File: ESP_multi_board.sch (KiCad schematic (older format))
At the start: 20 parts, among them P101 CONN_01X02, P102 CONN_01X06, P103 CONN_01X02, P104 CONN_01X06, P105 CONN_01X12, P106 CONN_01X03, P108 CONN_I2C_MPU6050, P109 CONN_01X03, P110 CONN_01X03, P111 CONN_DIGITAL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

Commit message: incluido DAC 4canales MCP4728, modificados conexion de motores para hacer pwm en los enables
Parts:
- removed P109, P110: CONN_01X03, Pin_Headers:Pin_Header_Straight_1x03, symbol CONN_01X03
- removed P111: CONN_DIGITAL, Pin_Headers:Pin_Header_Straight_1x10, symbol CONN_01X10
- removed P112: CONN_I2C, Pin_Headers:Pin_Header_Straight_1x04, symbol CONN_01X04
- added C?: CP, symbol CP
- added C?: 0.1u, symbol C
- added C?: 10u, symbol CP
- added P?: CONN_PWM_OUT, symbol CONN_01X04
- added P?: CONN_PWM_VCC, symbol CONN_01X04
- added P?: CONN_PWM_GND, symbol CONN_01X04
- added P?: CONN_PINES_DIG, symbol CONN_01X06
- added R?: 100k, symbol R
- added U?: MCP4728-E/UN, MSOP-10, symbol MCP4728-E/UN
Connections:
- net labels added: EN1, EN2
- wire segments 94 -> 110
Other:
- moved on the sheet: JP101, P106, P108, R101, R102, R103, R104, U102

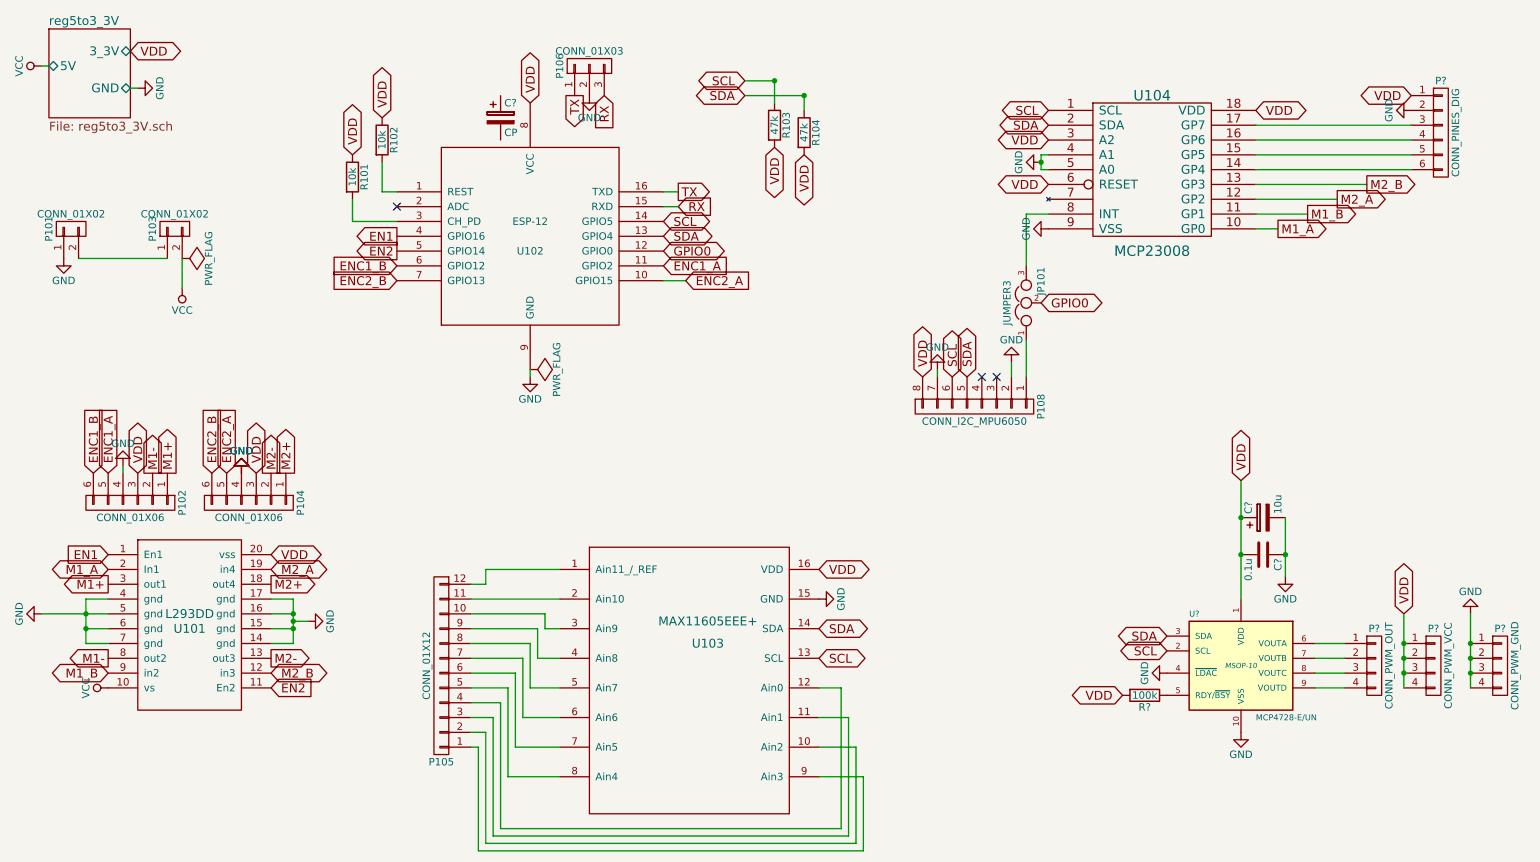
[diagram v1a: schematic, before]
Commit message: modificada huella del jumper, incluidos condensadores en la linea de 3.3v
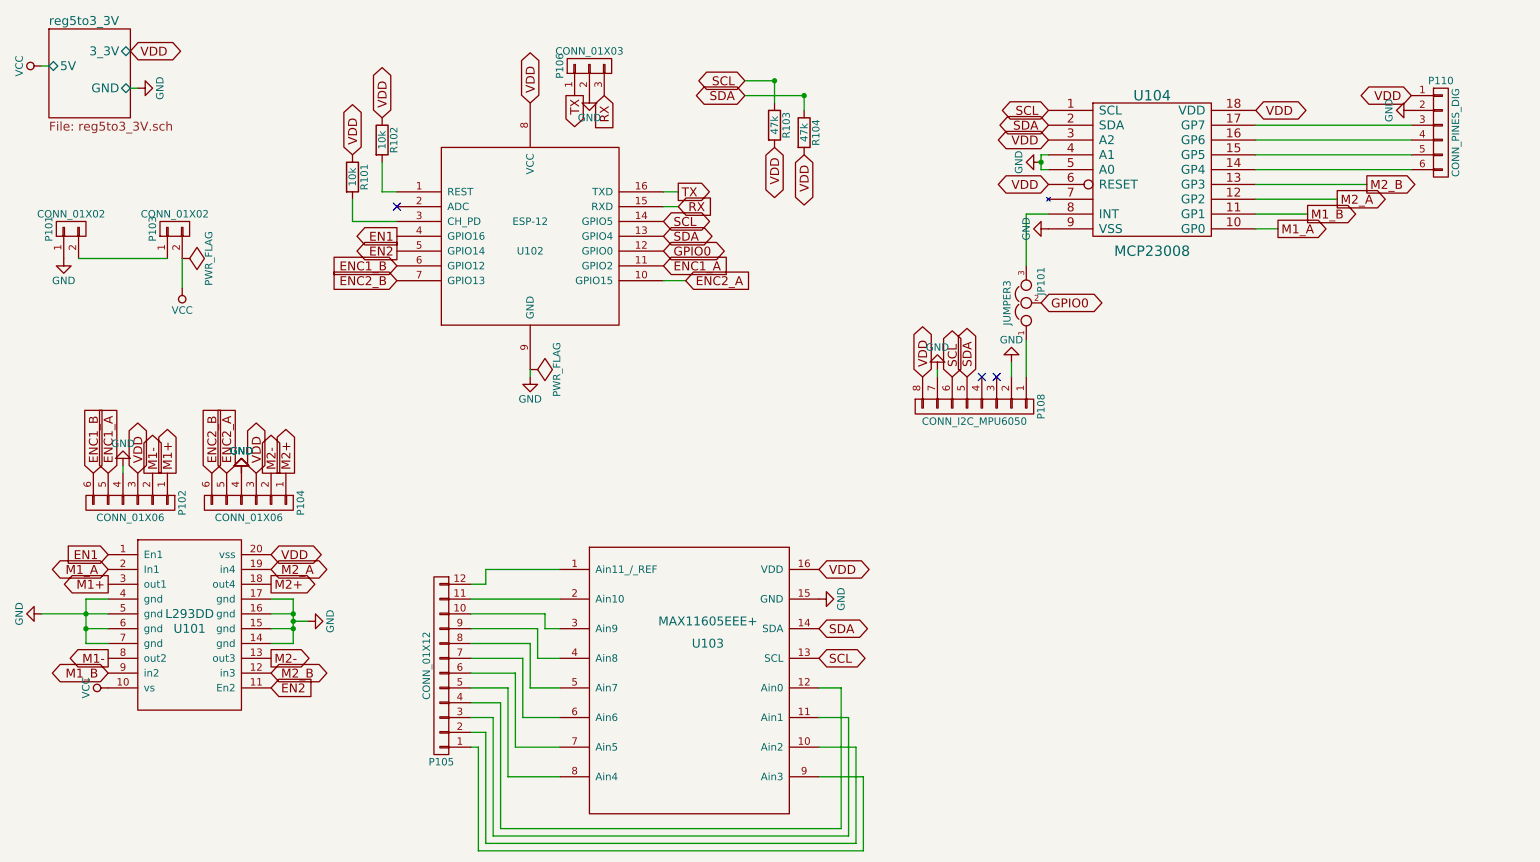
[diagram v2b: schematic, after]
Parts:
- removed C?: CP, symbol CP
- removed C?: 0.1u, symbol C
- removed C?: 10u, symbol CP
- removed P?: CONN_PWM_OUT, symbol CONN_01X04
- removed P?: CONN_PWM_VCC, symbol CONN_01X04
- removed P?: CONN_PWM_GND, symbol CONN_01X04
- removed R?: 100k, symbol R
- removed U?: MCP4728-E/UN, MSOP-10, symbol MCP4728-E/UN
- U103: footprint Housings_SSOP:QSOP-16_3.9x4.9mm_Pitch0.635mm -> Housings_SSOP:SSOP-16_5.3x6.2mm_Pitch0.65mm
- gave numbers to parts that had none: 1

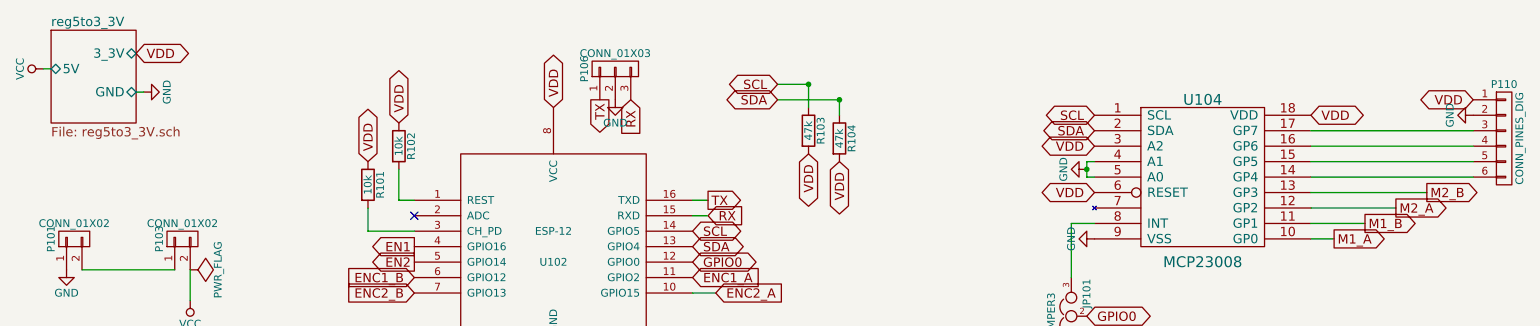
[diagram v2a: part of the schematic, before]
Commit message: autorouting generado con freerouting
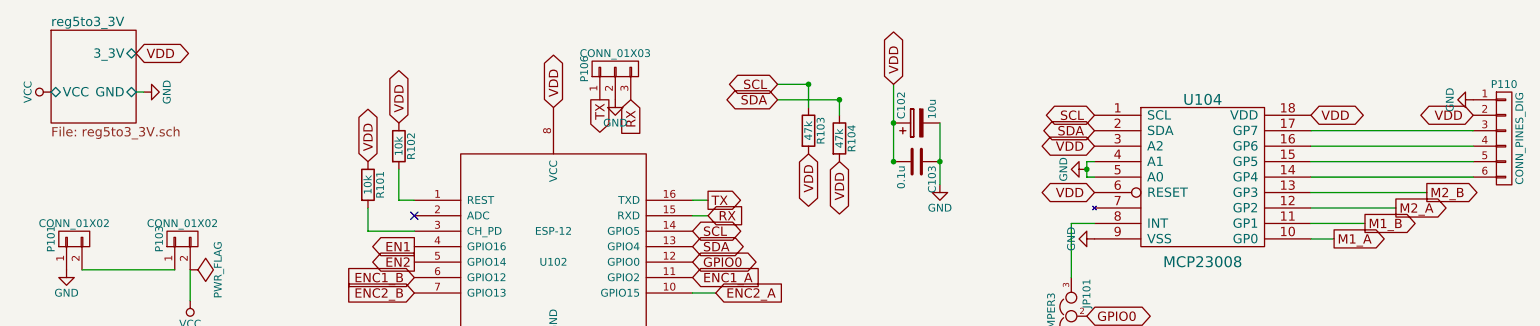
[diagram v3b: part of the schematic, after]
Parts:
- added C102: 10u, Capacitors_Tantalum_SMD:TantalC_SizeC_EIA-6032_HandSoldering, symbol CP
- added C103: 0.1u, Capacitors_SMD:C_0805_HandSoldering, symbol C
- JP101: footprint Oddities:NetTie-II_SMD -> keyboard_parts:SOLDER_JUMPER_3
- P110: footprint (none) -> Pin_Headers:Pin_Header_Straight_1x06
- R101, R102, R103, R104: footprint Resistors_SMD:R_1812_HandSoldering -> Resistors_SMD:R_0805_HandSoldering
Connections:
- net GND: now also P110.1 (P1), C102.2, C103.1; no longer P110.2 (P2)
- net VDD: now also P110.2 (P2), C102.1, C103.2; no longer P110.1 (P1)
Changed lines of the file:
@@
 L VCC #PWR06
 U 1 1 57125BE7
-P 950 1050
-F 0 "#PWR06" H 950 900 50  0001 C CNN
-F 1 "VCC" H 950 1200 50  0000 C CNN
-F 2 "" H 950 1050 50  0000 C CNN
-F 3 "" H 950 1050 50  0000 C CNN
-	1    950  1050
+P 1000 1200
+F 0 "#PWR06" H 1000 1050 50  0001 C CNN
+F 1 "VCC" H 1000 1350 50  0000 C CNN
+F 2 "" H 1000 1200 50  0000 C CNN
+F 3 "" H 1000 1200 50  0000 C CNN
+	1    1000 1200
 	0    -1   -1   0
 $EndComp
@@
 F1 "reg5to3_3V.sch" 60
 F2 "GND" B R 1550 1200 60
-F3 "5V" B L 1000 1050 60
-F4 "3_3V" B R 1550 950 60
+F3 "3_3V" B R 1550 950 60
+F4 "VCC" B L 1000 1200 60
 $EndSheet
 $Comp
@@
 F 0 "R102" V 3330 1550 50  0000 C CNN
 F 1 "10k" V 3250 1550 50  0000 C CNN
-F 2 "Resistors_SMD:R_1812_HandSoldering" V 3180 1550 50  0001 C CNN
+F 2 "Resistors_SMD:R_0805_HandSoldering" V 3180 1550 50  0001 C CNN
 F 3 "" H 3250 1550 50  0000 C CNN
 	1    3250 1550
@@
 F 0 "R101" V 3130 1800 50  0000 C CNN
 F 1 "10k" V 3050 1800 50  0000 C CNN
-F 2 "Resistors_SMD:R_1812_HandSoldering" V 2980 1800 50  0001 C CNN
+F 2 "Resistors_SMD:R_0805_HandSoldering" V 2980 1800 50  0001 C CNN
 F 3 "" H 3050 1800 50  0000 C CNN
 	1    3050 1800
@@
 F 0 "R104" V 6180 1500 50  0000 C CNN
 F 1 "47k" V 6100 1500 50  0000 C CNN
-F 2 "Resistors_SMD:R_1812_HandSoldering" V 6030 1500 50  0001 C CNN
+F 2 "Resistors_SMD:R_0805_HandSoldering" V 6030 1500 50  0001 C CNN
 F 3 "" H 6100 1500 50  0000 C CNN
 	1    6100 1500
@@
 F 0 "R103" V 5980 1450 50  0000 C CNN
 F 1 "47k" V 5900 1450 50  0000 C CNN
-F 2 "Resistors_SMD:R_1812_HandSoldering" V 5830 1450 50  0001 C CNN
+F 2 "Resistors_SMD:R_0805_HandSoldering" V 5830 1450 50  0001 C CNN
 F 3 "" H 5900 1450 50  0000 C CNN
 	1    5900 1450
@@
 Text GLabel 5150 2400 2    60   Input ~ 0
 ENC1_A
-Text GLabel 10200 1250 0    60   BiDi ~ 0
+Text GLabel 10200 1350 0    60   BiDi ~ 0
 VDD
 Text GLabel 1800 3800 1    60   Output ~ 0
@@
 L GND #PWR010
 U 1 1 57143D77
-P 10200 1350
-F 0 "#PWR010" H 10200 1100 50  0001 C CNN
-F 1 "GND" H 10200 1200 50  0000 C CNN
-F 2 "" H 10200 1350 50  0000 C CNN
-F 3 "" H 10200 1350 50  0000 C CNN
-	1    10200 1350
+P 10200 1250
+F 0 "#PWR010" H 10200 1000 50  0001 C CNN
+F 1 "GND" H 10200 1100 50  0000 C CNN
+F 2 "" H 10200 1250 50  0000 C CNN
+F 3 "" H 10200 1250 50  0000 C CNN
+	1    10200 1250
 	0    1    1    0
 $EndComp
@@
 	7600 2900 7600 3150
 Wire Wire Line
-	1000 1050 950  1050
-Wire Wire Line
 	1550 1200 1600 1200
 Wire Wire Line
@@
 F 0 "JP101" H 7650 2550 50  0000 L CNN
 F 1 "JUMPER3" H 7600 2750 50  0000 C BNN
-F 2 "Oddities:NetTie-II_SMD" H 7600 2650 50  0001 C CNN
+F 2 "keyboard_parts:SOLDER_JUMPER_3" H 7600 2650 50  0001 C CNN
 F 3 "" H 7600 2650 50  0000 C CNN
 	1    7600 2650
@@
 F 0 "P110" H 10400 1850 50  0000 C CNN
 F 1 "CONN_PINES_DIG" V 10500 1500 50  0000 C CNN
-F 2 "" H 10400 1500 50  0001 C CNN
+F 2 "Pin_Headers:Pin_Header_Straight_1x06" H 10400 1500 50  0001 C CNN
 F 3 "" H 10400 1500 50  0000 C CNN
 	1    10400 1500
 	1    0    0    -1
 $EndComp
+$Comp
+L GND #PWR021
+U 1 1 57154834
+P 6750 1800
+F 0 "#PWR021" H 6750 1550 50  0001 C CNN
+F 1 "GND" H 6750 1650 50  0000 C CNN
+F 2 "" H 6750 1800 50  0000 C CNN
+F 3 "" H 6750 1800 50  0000 C CNN
+	1    6750 1800
+	1    0    0    -1
+$EndComp
+Connection ~ 6750 1650
+Wire Wire Line
+	6750 1400 6750 1800
+Text GLabel 6450 1150 1    60   BiDi ~ 0
+VDD
+Connection ~ 6450 1400
+Connection ~ 6450 1650
+$Comp
+L CP C102
+U 1 1 5715447A
+P 6600 1400
+F 0 "C102" H 6625 1500 50  0000 L CNN
+F 1 "10u" H 6625 1300 50  0000 L CNN
+F 2 "Capacitors_Tantalum_SMD:TantalC_SizeC_EIA-6032_HandSoldering" H 6638 1250 50  0001 C CNN
+F 3 "" H 6600 1400 50  0000 C CNN
+	1    6600 1400
+	0    -1   -1   0
+$EndComp
+$Comp
+L C C103
+U 1 1 57154411
+P 6600 1650
+F 0 "C103" H 6625 1750 50  0000 L CNN
+F 1 "0.1u" H 6625 1550 50  0000 L CNN
+F 2 "Capacitors_SMD:C_0805_HandSoldering" H 6638 1500 50  0001 C CNN
+F 3 "" H 6600 1650 50  0000 C CNN
+	1    6600 1650
+	0    1    1    0
+$EndComp
+Wire Wire Line
+	6450 1150 6450 1650
 $EndSCHEMATC

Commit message: cambio de posiciones en la placa
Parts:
- C103: footprint Capacitors_SMD:C_0805_HandSoldering -> Capacitors_SMD:C_1206
- R101, R102, R103, R104: footprint Resistors_SMD:R_0805_HandSoldering -> Resistors_SMD:R_1206
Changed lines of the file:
@@
 F 0 "R102" V 3330 1550 50  0000 C CNN
 F 1 "10k" V 3250 1550 50  0000 C CNN
-F 2 "Resistors_SMD:R_0805_HandSoldering" V 3180 1550 50  0001 C CNN
+F 2 "Resistors_SMD:R_1206" V 3180 1550 50  0001 C CNN
 F 3 "" H 3250 1550 50  0000 C CNN
 	1    3250 1550
@@
 F 0 "R101" V 3130 1800 50  0000 C CNN
 F 1 "10k" V 3050 1800 50  0000 C CNN
-F 2 "Resistors_SMD:R_0805_HandSoldering" V 2980 1800 50  0001 C CNN
+F 2 "Resistors_SMD:R_1206" V 2980 1800 50  0001 C CNN
 F 3 "" H 3050 1800 50  0000 C CNN
 	1    3050 1800
@@
 F 0 "R104" V 6180 1500 50  0000 C CNN
 F 1 "47k" V 6100 1500 50  0000 C CNN
-F 2 "Resistors_SMD:R_0805_HandSoldering" V 6030 1500 50  0001 C CNN
+F 2 "Resistors_SMD:R_1206" V 6030 1500 50  0001 C CNN
 F 3 "" H 6100 1500 50  0000 C CNN
 	1    6100 1500
@@
 F 0 "R103" V 5980 1450 50  0000 C CNN
 F 1 "47k" V 5900 1450 50  0000 C CNN
-F 2 "Resistors_SMD:R_0805_HandSoldering" V 5830 1450 50  0001 C CNN
+F 2 "Resistors_SMD:R_1206" V 5830 1450 50  0001 C CNN
 F 3 "" H 5900 1450 50  0000 C CNN
 	1    5900 1450
@@
 F 0 "C103" H 6625 1750 50  0000 L CNN
 F 1 "0.1u" H 6625 1550 50  0000 L CNN
-F 2 "Capacitors_SMD:C_0805_HandSoldering" H 6638 1500 50  0001 C CNN
+F 2 "Capacitors_SMD:C_1206" H 6638 1500 50  0001 C CNN
 F 3 "" H 6600 1650 50  0000 C CNN
 	1    6600 1650

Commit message: versión quasifinal
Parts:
- added R103, R104: 10k, Resistors_SMD:R_1206, symbol R
- added SW101, SW102: SW_PUSH_SMALL, Buttons_Switches_SMD:SW_SPST_EVPBF, symbol SW_PUSH_SMALL
- renumbered C102 to C101, C103 to C102, P108 to P107, P110 to P108, R103 to R105, R104 to R106
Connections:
- net EN1: now also U102.11 (GPIO2); no longer U102.4 (GPIO16)
- net EN2: now also U102.14 (GPIO5); no longer U102.5 (GPIO14)
- net ENC1_A: now also U102.4 (GPIO16); no longer U102.11 (GPIO2)
- net ENC2_A: now also U102.5 (GPIO14); no longer U102.10 (GPIO15)
- net GND: now also R103.2, SW101.2, SW102.2
- net GPIO0: now also U102.10 (GPIO15), R103.1; no longer U102.12 (GPIO0)
- net SCL: now also U102.12 (GPIO0), R104.2, SW102.1; no longer U102.14 (GPIO5)
- net VDD: now also R104.1
- net at R102.2, U102.1 (REST): now also SW101.1
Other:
- moved on the sheet: R101
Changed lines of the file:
@@
-$EndComp
-$Comp
-L ESP-12 U102
-U 1 1 57125BD1
-P 4250 2200
-F 0 "U102" H 4250 2100 50  0000 C CNN
-F 1 "ESP-12" H 4250 2300 50  0000 C CNN
-F 2 "ESP8266:ESP-12" H 4250 2200 50  0001 C CNN
-F 3 "" H 4250 2200 50  0001 C CNN
-	1    4250 2200
-	1    0    0    -1
 $EndComp
 $Comp
@@
 SDA
 Text GLabel 7750 1350 0    60   BiDi ~ 0
-SCL
-Text GLabel 5150 2100 2    60   BiDi ~ 0
 SCL
 Text GLabel 5150 2200 2    60   BiDi ~ 0
@@
 Text GLabel 7750 1550 0    60   BiDi ~ 0
 VDD
-Text GLabel 5150 2300 2    60   BiDi ~ 0
+Text GLabel 5300 2500 2    60   BiDi ~ 0
 GPIO0
 $Comp
@@
 L R R101
 U 1 1 57127BE5
-P 3050 1800
-F 0 "R101" V 3130 1800 50  0000 C CNN
-F 1 "10k" V 3050 1800 50  0000 C CNN
-F 2 "Resistors_SMD:R_1206" V 2980 1800 50  0001 C CNN
-F 3 "" H 3050 1800 50  0000 C CNN
-	1    3050 1800
+P 2600 1950
+F 0 "R101" V 2680 1950 50  0000 C CNN
+F 1 "10k" V 2600 1950 50  0000 C CNN
+F 2 "Resistors_SMD:R_1206" V 2530 1950 50  0001 C CNN
+F 3 "" H 2600 1950 50  0000 C CNN
+	1    2600 1950
 	1    0    0    -1
 $EndComp
 Text GLabel 3250 1400 1    60   BiDi ~ 0
 VDD
-Text GLabel 3050 1650 1    60   BiDi ~ 0
+Text GLabel 2600 1800 1    60   BiDi ~ 0
 VDD
 Text GLabel 5250 2000 2    60   Input ~ 0
@@
 TX
 $Comp
-L R R104
+L R R106
 U 1 1 5712A472
 P 6100 1500
-F 0 "R104" V 6180 1500 50  0000 C CNN
+F 0 "R106" V 6180 1500 50  0000 C CNN
 F 1 "47k" V 6100 1500 50  0000 C CNN
 F 2 "Resistors_SMD:R_1206" V 6030 1500 50  0001 C CNN
@@
 VDD
 $Comp
-L R R103
+L R R105
 U 1 1 5712A576
 P 5900 1450
-F 0 "R103" V 5980 1450 50  0000 C CNN
+F 0 "R105" V 5980 1450 50  0000 C CNN
 F 1 "47k" V 5900 1450 50  0000 C CNN
 F 2 "Resistors_SMD:R_1206" V 5830 1450 50  0001 C CNN
@@
 SCL
 $Comp
-L CONN_01X08 P108
+L CONN_01X08 P107
 U 1 1 5713D03F
 P 7250 3350
-F 0 "P108" H 7250 3800 50  0000 C CNN
+F 0 "P107" H 7250 3800 50  0000 C CNN
 F 1 "CONN_I2C_MPU6050" V 7350 3350 50  0000 C CNN
 F 2 "Pin_Headers:Pin_Header_Straight_1x08" H 7250 3350 50  0001 C CNN
@@
 Text GLabel 7750 1850 0    60   BiDi ~ 0
 VDD
-Text GLabel 5300 2500 2    60   Input ~ 0
+Text GLabel 3350 2300 0    60   Input ~ 0
 ENC2_A
-Text GLabel 5150 2400 2    60   Input ~ 0
+Text GLabel 3350 2200 0    60   Input ~ 0
 ENC1_A
 Text GLabel 10200 1350 0    60   BiDi ~ 0
@@
 	3250 1900 3350 1900
 Wire Wire Line
-	3350 2100 3050 2100
-Wire Wire Line
-	3050 2100 3050 1950
+	2600 2100 3350 2100
 Wire Wire Line
 	5700 1250 6100 1250
@@
 NoConn ~ 7300 3150
 NoConn ~ 7400 3150
-Text GLabel 3350 2200 0    60   Output ~ 0
+Text GLabel 5150 2400 2    60   Output ~ 0
 EN1
-Text GLabel 3350 2300 0    60   Output ~ 0
+Text GLabel 5150 2100 2    60   Output ~ 0
 EN2
 Text GLabel 3350 2400 0    60   Input ~ 0
@@
 M2_B
 $Comp
-L CONN_01X06 P110
+L CONN_01X06 P108
 U 1 1 571568CA
 P 10400 1500
-F 0 "P110" H 10400 1850 50  0000 C CNN
+F 0 "P108" H 10400 1850 50  0000 C CNN
 F 1 "CONN_PINES_DIG" V 10500 1500 50  0000 C CNN
 F 2 "Pin_Headers:Pin_Header_Straight_1x06" H 10400 1500 50  0001 C CNN
@@
 Connection ~ 6450 1650
 $Comp
-L CP C102
+L CP C101
 U 1 1 5715447A
 P 6600 1400
-F 0 "C102" H 6625 1500 50  0000 L CNN
+F 0 "C101" H 6625 1500 50  0000 L CNN
 F 1 "10u" H 6625 1300 50  0000 L CNN
 F 2 "Capacitors_Tantalum_SMD:TantalC_SizeC_EIA-6032_HandSoldering" H 6638 1250 50  0001 C CNN
@@
 $EndComp
 $Comp
-L C C103
+L C C102
 U 1 1 57154411
 P 6600 1650
-F 0 "C103" H 6625 1750 50  0000 L CNN
+F 0 "C102" H 6625 1750 50  0000 L CNN
 F 1 "0.1u" H 6625 1550 50  0000 L CNN
 F 2 "Capacitors_SMD:C_1206" H 6638 1500 50  0001 C CNN
@@
 Wire Wire Line
 	6450 1150 6450 1650
+Wire Wire Line
+	5150 2300 5950 2300
+$Comp
+L R R104
+U 1 1 5719126A
+P 5600 2150
+F 0 "R104" V 5680 2150 50  0000 C CNN
+F 1 "10k" V 5600 2150 50  0000 C CNN
+F 2 "Resistors_SMD:R_1206" V 5530 2150 50  0001 C CNN
+F 3 "" H 5600 2150 50  0000 C CNN
+	1    5600 2150
+	1    0    0    -1
+$EndComp
+Text GLabel 5600 2000 1    60   BiDi ~ 0
+VDD
+$Comp
+L SW_PUSH_SMALL SW102
+U 1 1 5719131F
+P 5900 2400
+F 0 "SW102" H 6050 2510 50  0000 C CNN
+F 1 "SW_PUSH_SMALL" H 5900 2321 50  0000 C CNN
+F 2 "Buttons_Switches_SMD:SW_SPST_EVPBF" H 5900 2400 50  0001 C CNN
+F 3 "" H 5900 2400 50  0000 C CNN
+	1    5900 2400
+	1    0    0    -1
+$EndComp
+$Comp
+L GND #PWR022
+U 1 1 571913A6
+P 6000 2500
+F 0 "#PWR022" H 6000 2250 50  0001 C CNN
+F 1 "GND" H 6000 2350 50  0000 C CNN
+F 2 "" H 6000 2500 50  0000 C CNN
+F 3 "" H 6000 2500 50  0000 C CNN
+	1    6000 2500
+	1    0    0    -1
+$EndComp
+$Comp
+L R R103
+U 1 1 57191663
+P 5150 2650
+F 0 "R103" V 5230 2650 50  0000 C CNN
+F 1 "10k" V 5150 2650 50  0000 C CNN
+F 2 "Resistors_SMD:R_1206" V 5080 2650 50  0001 C CNN
+F 3 "" H 5150 2650 50  0000 C CNN
+	1    5150 2650
+	1    0    0    -1
+$EndComp
+$Comp
+L GND #PWR023
+U 1 1 571916BE
+P 5150 2800
+F 0 "#PWR023" H 5150 2550 50  0001 C CNN
+F 1 "GND" H 5150 2650 50  0000 C CNN
+F 2 "" H 5150 2800 50  0000 C CNN
+F 3 "" H 5150 2800 50  0000 C CNN
+	1    5150 2800
+	1    0    0    -1
+$EndComp
+$Comp
+L ESP-12 U102
+U 1 1 57125BD1
+P 4250 2200
+F 0 "U102" H 4250 2100 50  0000 C CNN
+F 1 "ESP-12" H 4250 2300 50  0000 C CNN
+F 2 "ESP8266:ESP-12" H 4250 2200 50  0001 C CNN
+F 3 "" H 4250 2200 50  0001 C CNN
+	1    4250 2200
+	1    0    0    -1
+$EndComp
+Text GLabel 5950 2300 2    60   BiDi ~ 0
+SCL
+$Comp
+L SW_PUSH_SMALL SW101
+U 1 1 57213D89
+P 3150 1800
+F 0 "SW101" H 3300 1910 50  0000 C CNN
+F 1 "SW_PUSH_SMALL" H 3150 1721 50  0000 C CNN
+F 2 "Buttons_Switches_SMD:SW_SPST_EVPBF" H 3150 1800 50  0001 C CNN
+F 3 "" H 3150 1800 50  0000 C CNN
+	1    3150 1800
+	-1   0    0    1
+$EndComp
+$Comp
+L GND #PWR024
+U 1 1 57213D8F
+P 3050 1700
+F 0 "#PWR024" H 3050 1450 50  0001 C CNN
+F 1 "GND" H 3050 1550 50  0000 C CNN
+F 2 "" H 3050 1700 50  0000 C CNN
+F 3 "" H 3050 1700 50  0000 C CNN
+	1    3050 1700
+	-1   0    0    1
+$EndComp
+Connection ~ 5600 2300
+Connection ~ 5800 2300
 $EndSCHEMATC
